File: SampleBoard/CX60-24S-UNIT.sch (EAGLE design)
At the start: 5 parts, among them CN1 CX60-24S-UNIT, CN2 87520-0010BLF, CN3 IF_5PIN_H

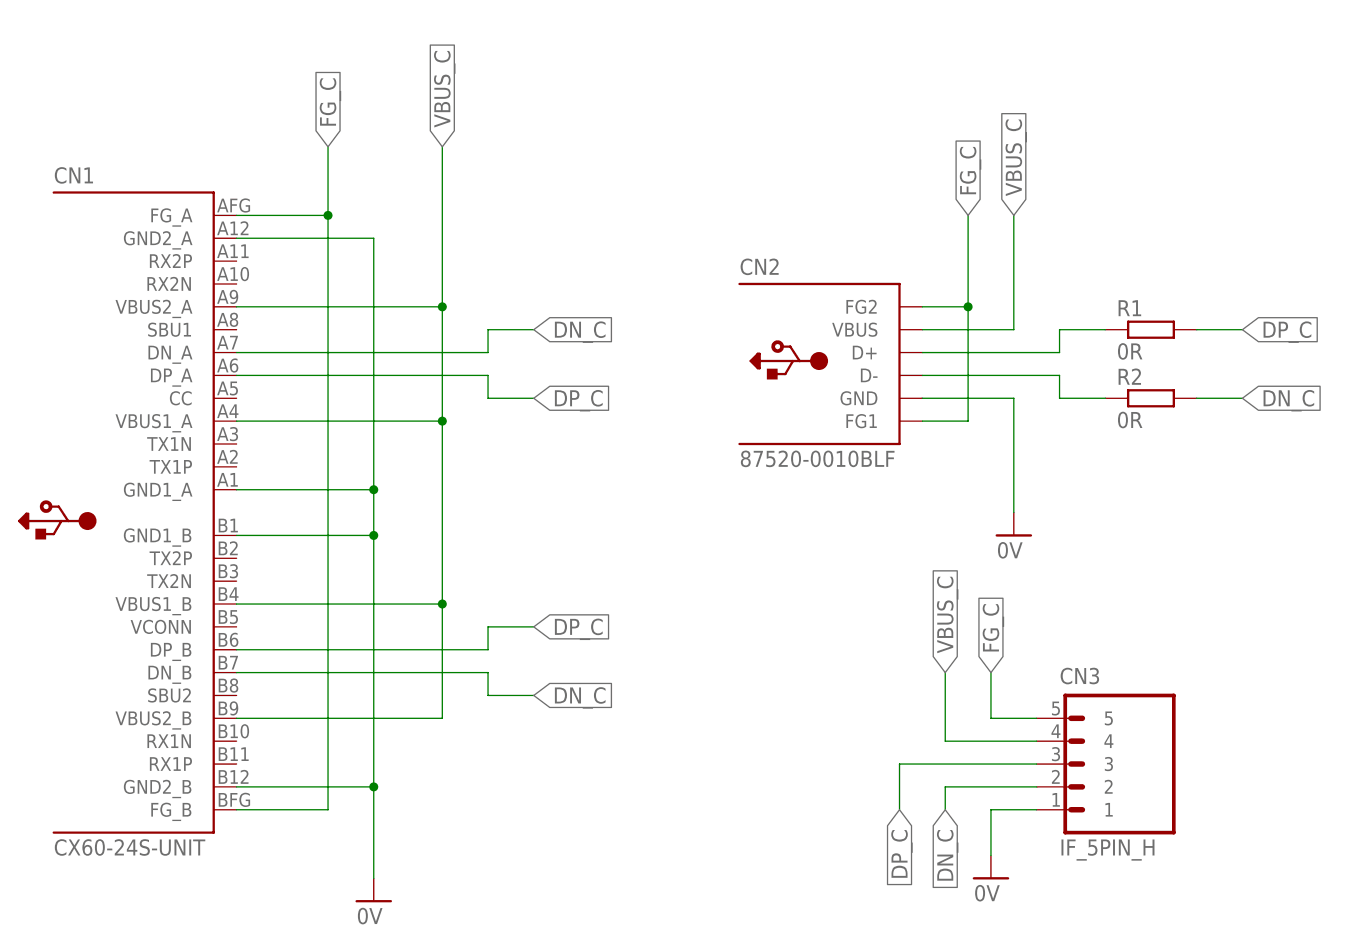
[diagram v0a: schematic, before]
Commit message: 評価用基板を修正
・CCの配線（プルダウン抵抗）が抜けていたので追加
・テスト用ホールの位置を修正
・プラグB面のD+、D-は不要なので削除
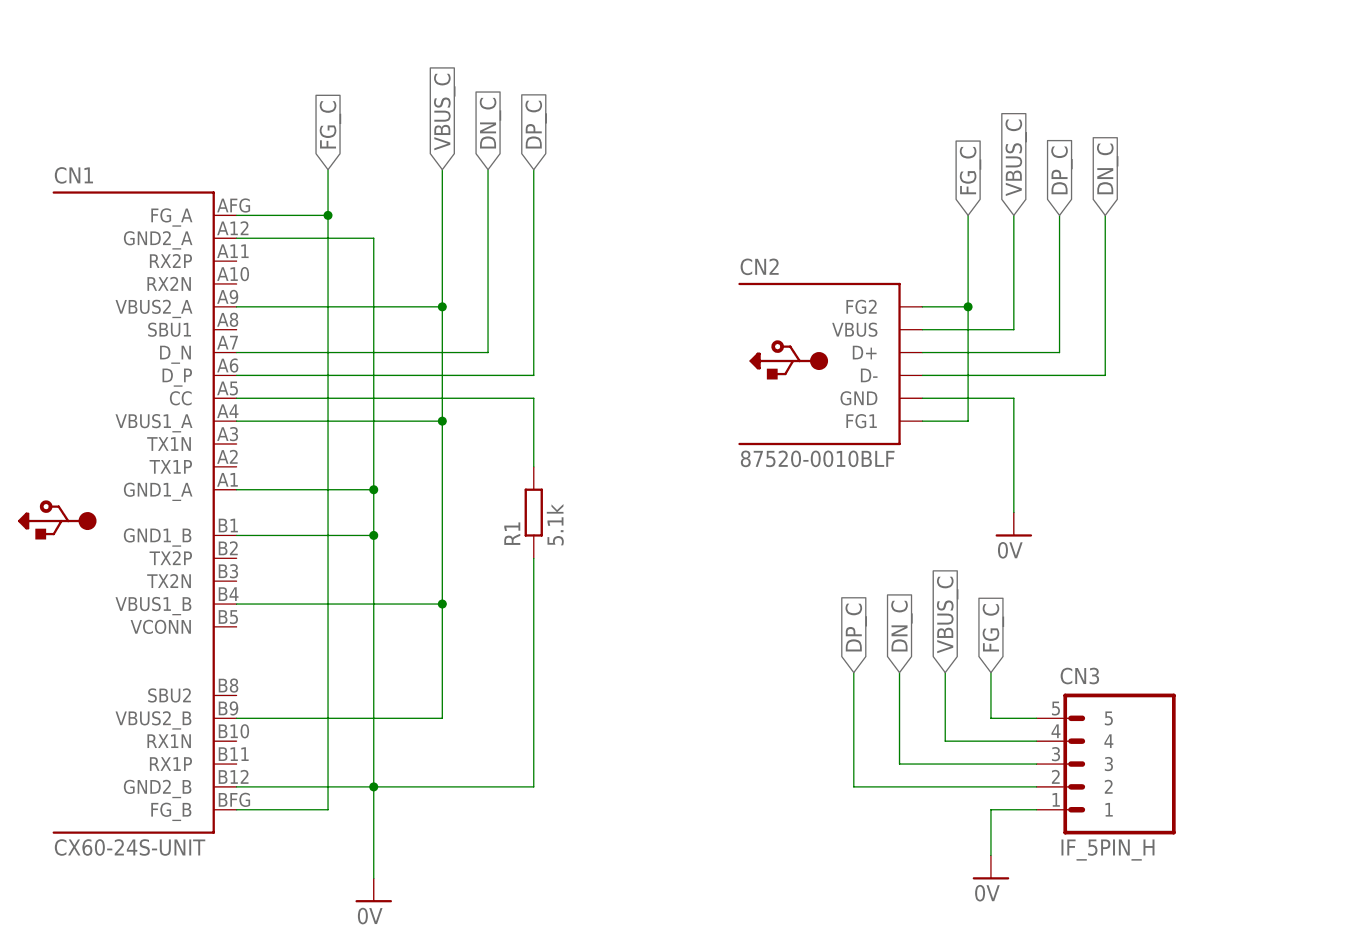
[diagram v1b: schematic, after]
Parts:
- removed R2: 0R, Parts:RESISTOR_300MIL
- R1: value 0R -> 5.1k; device Parts:RESISTOR_300MIL -> Parts:RESISTOR_0402
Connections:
- removed net N$1: CN2.D-, R2.1
- removed net N$2: CN2.D+, R1.1
- new net N$3: CN1.CC, R1.2
- net 0V: now also R1.1
- net DN_C: now also CN1.D_N, CN2.D-, CN3.3; no longer CN1.DN_A, CN1.DN_B, CN3.2, R2.2
- net DP_C: now also CN1.D_P, CN2.D+, CN3.2; no longer CN1.DP_A, CN1.DP_B, CN3.3, R1.2
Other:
- moved on the sheet: R1
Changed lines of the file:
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@@
 <setting verticaltext="up"/>
 </settings>
-<grid distance="0.1" unitdist="inch" unit="inch" style="lines" multiple="1" display="yes" altdistance="0.01" altunitdist="inch" altunit="inch"/>
+<grid distance="0.1" unitdist="inch" unit="inch" style="lines" multiple="1" display="no" altdistance="0.01" altunitdist="inch" altunit="inch"/>
 <layers>
 <layer number="1" name="Top" color="4" fill="1" visible="no" active="no"/>
@@
 <part name="CN1" library="Connectors" deviceset="CX60-24S-UNIT" device=""/>
 <part name="CN2" library="Connectors" deviceset="87520-0010BLF" device=""/>
-<part name="R1" library="Parts" deviceset="RESISTOR" device="_300MIL" value="0R"/>
-<part name="R2" library="Parts" deviceset="RESISTOR" device="_300MIL" value="0R"/>
 <part name="GND1" library="Supply" deviceset="0V" device=""/>
 <part name="GND2" library="Supply" deviceset="0V" device=""/>
 <part name="CN3" library="Connectors" deviceset="IF_5PIN" device="_H"/>
 <part name="GND3" library="Supply" deviceset="0V" device=""/>
+<part name="R1" library="Parts" deviceset="RESISTOR" device="_0402" value="5.1k"/>
 </parts>
 <sheets>
@@
 <instance part="CN1" gate="G$1" x="63.5" y="93.98"/>
 <instance part="CN2" gate="G$1" x="139.7" y="101.6"/>
-<instance part="R1" gate="G$1" x="180.34" y="114.3"/>
-<instance part="R2" gate="G$1" x="180.34" y="106.68"/>
 <instance part="GND1" gate="1" x="170.18" y="91.44"/>
 <instance part="GND2" gate="1" x="99.06" y="50.8"/>
 <instance part="CN3" gate="G$1" x="172.72" y="71.12"/>
 <instance part="GND3" gate="1" x="167.64" y="53.34"/>
+<instance part="R1" gate="G$1" x="116.84" y="88.9" rot="R90"/>
 </instances>
 <busses>
@@
 <wire x1="99.06" y1="124.46" x2="99.06" y2="96.52" width="0.1524" layer="91"/>
 <junction x="99.06" y="96.52"/>
+<pinref part="R1" gate="G$1" pin="1"/>
+<wire x1="116.84" y1="88.9" x2="116.84" y2="63.5" width="0.1524" layer="91"/>
+<wire x1="116.84" y1="63.5" x2="99.06" y2="63.5" width="0.1524" layer="91"/>
 </segment>
 <segment>
@@
 </segment>
 </net>
-<net name="N$1" class="0">
-<segment>
-<pinref part="CN2" gate="G$1" pin="D-"/>
-<wire x1="160.02" y1="109.22" x2="175.26" y2="109.22" width="0.1524" layer="91"/>
-<wire x1="175.26" y1="109.22" x2="175.26" y2="106.68" width="0.1524" layer="91"/>
-<pinref part="R2" gate="G$1" pin="1"/>
-<wire x1="175.26" y1="106.68" x2="180.34" y2="106.68" width="0.1524" layer="91"/>
-</segment>
-</net>
-<net name="N$2" class="0">
+<net name="DP_C" class="0">
 <segment>
 <pinref part="CN2" gate="G$1" pin="D+"/>
 <wire x1="160.02" y1="111.76" x2="175.26" y2="111.76" width="0.1524" layer="91"/>
-<wire x1="175.26" y1="111.76" x2="175.26" y2="114.3" width="0.1524" layer="91"/>
-<pinref part="R1" gate="G$1" pin="1"/>
-<wire x1="175.26" y1="114.3" x2="180.34" y2="114.3" width="0.1524" layer="91"/>
-</segment>
-</net>
-<net name="DP_C" class="0">
-<segment>
-<pinref part="R1" gate="G$1" pin="2"/>
-<wire x1="190.5" y1="114.3" x2="195.58" y2="114.3" width="0.1524" layer="91"/>
-<label x="195.58" y="114.3" size="1.778" layer="95" xref="yes"/>
-</segment>
-<segment>
-<pinref part="CN1" gate="G$1" pin="DP_A"/>
-<wire x1="83.82" y1="109.22" x2="111.76" y2="109.22" width="0.1524" layer="91"/>
-<label x="116.84" y="106.68" size="1.778" layer="95" xref="yes"/>
-<wire x1="111.76" y1="109.22" x2="111.76" y2="106.68" width="0.1524" layer="91"/>
-<wire x1="111.76" y1="106.68" x2="116.84" y2="106.68" width="0.1524" layer="91"/>
-</segment>
-<segment>
-<pinref part="CN1" gate="G$1" pin="DP_B"/>
-<wire x1="83.82" y1="78.74" x2="111.76" y2="78.74" width="0.1524" layer="91"/>
-<wire x1="111.76" y1="78.74" x2="111.76" y2="81.28" width="0.1524" layer="91"/>
-<wire x1="111.76" y1="81.28" x2="116.84" y2="81.28" width="0.1524" layer="91"/>
-<label x="116.84" y="81.28" size="1.778" layer="95" xref="yes"/>
+<wire x1="175.26" y1="111.76" x2="175.26" y2="127" width="0.1524" layer="91"/>
+<label x="175.26" y="127" size="1.778" layer="95" rot="R90" xref="yes"/>
+</segment>
+<segment>
+<pinref part="CN1" gate="G$1" pin="D_P"/>
+<wire x1="83.82" y1="109.22" x2="116.84" y2="109.22" width="0.1524" layer="91"/>
+<wire x1="116.84" y1="109.22" x2="116.84" y2="132.08" width="0.1524" layer="91"/>
+<label x="116.84" y="132.08" size="1.778" layer="95" rot="R90" xref="yes"/>
+</segment>
+<segment>
+<pinref part="CN3" gate="G$1" pin="2"/>
+<wire x1="172.72" y1="63.5" x2="152.4" y2="63.5" width="0.1524" layer="91"/>
+<wire x1="152.4" y1="63.5" x2="152.4" y2="76.2" width="0.1524" layer="91"/>
+<label x="152.4" y="76.2" size="1.778" layer="95" rot="R90" xref="yes"/>
+</segment>
+</net>
+<net name="DN_C" class="0">
+<segment>
+<pinref part="CN1" gate="G$1" pin="D_N"/>
+<wire x1="83.82" y1="111.76" x2="111.76" y2="111.76" width="0.1524" layer="91"/>
+<wire x1="111.76" y1="111.76" x2="111.76" y2="132.08" width="0.1524" layer="91"/>
+<label x="111.76" y="132.08" size="1.778" layer="95" rot="R90" xref="yes"/>
+</segment>
+<segment>
+<pinref part="CN2" gate="G$1" pin="D-"/>
+<wire x1="160.02" y1="109.22" x2="180.34" y2="109.22" width="0.1524" layer="91"/>
+<wire x1="180.34" y1="109.22" x2="180.34" y2="127" width="0.1524" layer="91"/>
+<label x="180.34" y="127" size="1.778" layer="95" rot="R90" xref="yes"/>
 </segment>
 <segment>
 <pinref part="CN3" gate="G$1" pin="3"/>
 <wire x1="172.72" y1="66.04" x2="157.48" y2="66.04" width="0.1524" layer="91"/>
-<wire x1="157.48" y1="66.04" x2="157.48" y2="60.96" width="0.1524" layer="91"/>
-<label x="157.48" y="60.96" size="1.778" layer="95" rot="R270" xref="yes"/>
-</segment>
-</net>
-<net name="DN_C" class="0">
-<segment>
-<pinref part="R2" gate="G$1" pin="2"/>
-<wire x1="190.5" y1="106.68" x2="195.58" y2="106.68" width="0.1524" layer="91"/>
-<label x="195.58" y="106.68" size="1.778" layer="95" xref="yes"/>
-</segment>
-<segment>
-<pinref part="CN1" gate="G$1" pin="DN_A"/>
-<wire x1="83.82" y1="111.76" x2="111.76" y2="111.76" width="0.1524" layer="91"/>
-<label x="116.84" y="114.3" size="1.778" layer="95" xref="yes"/>
-<wire x1="111.76" y1="111.76" x2="111.76" y2="114.3" width="0.1524" layer="91"/>
-<wire x1="111.76" y1="114.3" x2="116.84" y2="114.3" width="0.1524" layer="91"/>
-</segment>
-<segment>
-<pinref part="CN1" gate="G$1" pin="DN_B"/>
-<wire x1="83.82" y1="76.2" x2="111.76" y2="76.2" width="0.1524" layer="91"/>
-<wire x1="111.76" y1="76.2" x2="111.76" y2="73.66" width="0.1524" layer="91"/>
-<wire x1="111.76" y1="73.66" x2="116.84" y2="73.66" width="0.1524" layer="91"/>
-<label x="116.84" y="73.66" size="1.778" layer="95" xref="yes"/>
-</segment>
-<segment>
-<pinref part="CN3" gate="G$1" pin="2"/>
-<wire x1="172.72" y1="63.5" x2="162.56" y2="63.5" width="0.1524" layer="91"/>
-<wire x1="162.56" y1="63.5" x2="162.56" y2="60.96" width="0.1524" layer="91"/>
-<label x="162.56" y="60.96" size="1.778" layer="95" rot="R270" xref="yes"/>
+<wire x1="157.48" y1="66.04" x2="157.48" y2="76.2" width="0.1524" layer="91"/>
+<label x="157.48" y="76.2" size="1.778" layer="95" rot="R90" xref="yes"/>
 </segment>
 </net>
@@
 <wire x1="83.82" y1="71.12" x2="106.68" y2="71.12" width="0.1524" layer="91"/>
 <wire x1="106.68" y1="71.12" x2="106.68" y2="83.82" width="0.1524" layer="91"/>
-<label x="106.68" y="134.62" size="1.778" layer="95" rot="R90" xref="yes"/>
+<label x="106.68" y="132.08" size="1.778" layer="95" rot="R90" xref="yes"/>
 <pinref part="CN1" gate="G$1" pin="VBUS1_B"/>
 <wire x1="106.68" y1="83.82" x2="106.68" y2="104.14" width="0.1524" layer="91"/>
 <wire x1="106.68" y1="104.14" x2="106.68" y2="116.84" width="0.1524" layer="91"/>
-<wire x1="106.68" y1="116.84" x2="106.68" y2="134.62" width="0.1524" layer="91"/>
+<wire x1="106.68" y1="116.84" x2="106.68" y2="132.08" width="0.1524" layer="91"/>
 <wire x1="83.82" y1="83.82" x2="106.68" y2="83.82" width="0.1524" layer="91"/>
 <junction x="106.68" y="83.82"/>
@@
 <pinref part="CN1" gate="G$1" pin="FG_A"/>
 <wire x1="83.82" y1="127" x2="93.98" y2="127" width="0.1524" layer="91"/>
-<wire x1="93.98" y1="127" x2="93.98" y2="134.62" width="0.1524" layer="91"/>
-<label x="93.98" y="134.62" size="1.778" layer="95" rot="R90" xref="yes"/>
+<wire x1="93.98" y1="127" x2="93.98" y2="132.08" width="0.1524" layer="91"/>
+<label x="93.98" y="132.08" size="1.778" layer="95" rot="R90" xref="yes"/>
 <pinref part="CN1" gate="G$1" pin="FG_B"/>
 <wire x1="83.82" y1="60.96" x2="93.98" y2="60.96" width="0.1524" layer="91"/>
@@
 </segment>
 </net>
+<net name="N$3" class="0">
+<segment>
+<pinref part="CN1" gate="G$1" pin="CC"/>
+<wire x1="83.82" y1="106.68" x2="116.84" y2="106.68" width="0.1524" layer="91"/>
+<wire x1="116.84" y1="106.68" x2="116.84" y2="99.06" width="0.1524" layer="91"/>
+<pinref part="R1" gate="G$1" pin="2"/>
+</segment>
+</net>

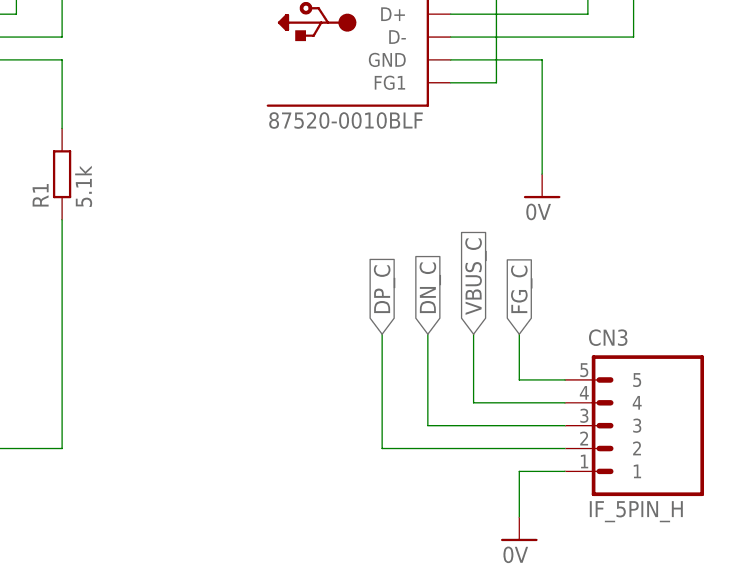
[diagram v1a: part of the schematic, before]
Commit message: 評価用基板を修正
・配線パターンを修正
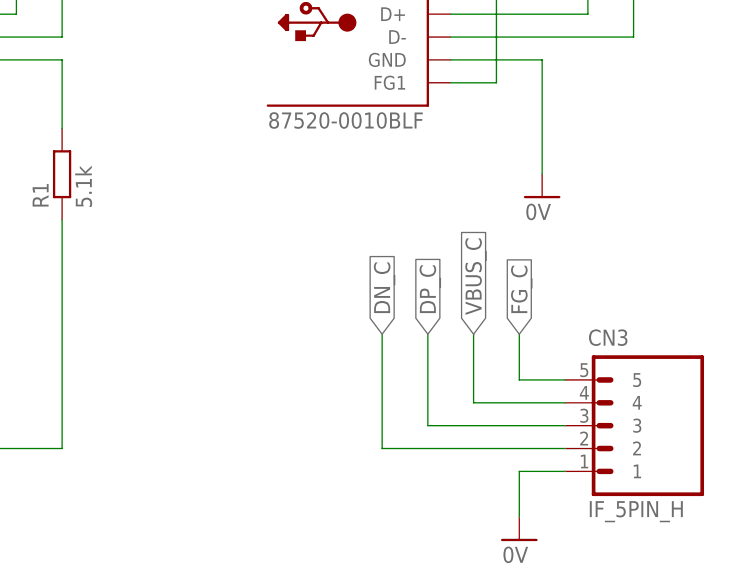
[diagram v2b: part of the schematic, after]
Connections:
- net DN_C: now also CN3.2; no longer CN3.3
- net DP_C: now also CN3.3; no longer CN3.2
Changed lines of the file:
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@@
 <setting verticaltext="up"/>
 </settings>
-<grid distance="0.1" unitdist="inch" unit="inch" style="lines" multiple="1" display="no" altdistance="0.01" altunitdist="inch" altunit="inch"/>
+<grid distance="0.1" unitdist="inch" unit="inch" style="lines" multiple="1" display="yes" altdistance="0.01" altunitdist="inch" altunit="inch"/>
 <layers>
 <layer number="1" name="Top" color="4" fill="1" visible="no" active="no"/>
@@
 </segment>
 <segment>
+<pinref part="CN3" gate="G$1" pin="3"/>
+<wire x1="172.72" y1="66.04" x2="157.48" y2="66.04" width="0.1524" layer="91"/>
+<wire x1="157.48" y1="66.04" x2="157.48" y2="76.2" width="0.1524" layer="91"/>
+<label x="157.48" y="76.2" size="1.778" layer="95" rot="R90" xref="yes"/>
+</segment>
+</net>
+<net name="DN_C" class="0">
+<segment>
+<pinref part="CN1" gate="G$1" pin="D_N"/>
+<wire x1="83.82" y1="111.76" x2="111.76" y2="111.76" width="0.1524" layer="91"/>
+<wire x1="111.76" y1="111.76" x2="111.76" y2="132.08" width="0.1524" layer="91"/>
+<label x="111.76" y="132.08" size="1.778" layer="95" rot="R90" xref="yes"/>
+</segment>
+<segment>
+<pinref part="CN2" gate="G$1" pin="D-"/>
+<wire x1="160.02" y1="109.22" x2="180.34" y2="109.22" width="0.1524" layer="91"/>
+<wire x1="180.34" y1="109.22" x2="180.34" y2="127" width="0.1524" layer="91"/>
+<label x="180.34" y="127" size="1.778" layer="95" rot="R90" xref="yes"/>
+</segment>
+<segment>
 <pinref part="CN3" gate="G$1" pin="2"/>
 <wire x1="172.72" y1="63.5" x2="152.4" y2="63.5" width="0.1524" layer="91"/>
@@
 </segment>
 </net>
-<net name="DN_C" class="0">
-<segment>
-<pinref part="CN1" gate="G$1" pin="D_N"/>
-<wire x1="83.82" y1="111.76" x2="111.76" y2="111.76" width="0.1524" layer="91"/>
-<wire x1="111.76" y1="111.76" x2="111.76" y2="132.08" width="0.1524" layer="91"/>
-<label x="111.76" y="132.08" size="1.778" layer="95" rot="R90" xref="yes"/>
-</segment>
-<segment>
-<pinref part="CN2" gate="G$1" pin="D-"/>
-<wire x1="160.02" y1="109.22" x2="180.34" y2="109.22" width="0.1524" layer="91"/>
-<wire x1="180.34" y1="109.22" x2="180.34" y2="127" width="0.1524" layer="91"/>
-<label x="180.34" y="127" size="1.778" layer="95" rot="R90" xref="yes"/>
-</segment>
-<segment>
-<pinref part="CN3" gate="G$1" pin="3"/>
-<wire x1="172.72" y1="66.04" x2="157.48" y2="66.04" width="0.1524" layer="91"/>
-<wire x1="157.48" y1="66.04" x2="157.48" y2="76.2" width="0.1524" layer="91"/>
-<label x="157.48" y="76.2" size="1.778" layer="95" rot="R90" xref="yes"/>
-</segment>
-</net>
